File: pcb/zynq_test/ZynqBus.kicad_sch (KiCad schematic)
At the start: 22 parts, among them U202 XC7Z020-2CLG400I

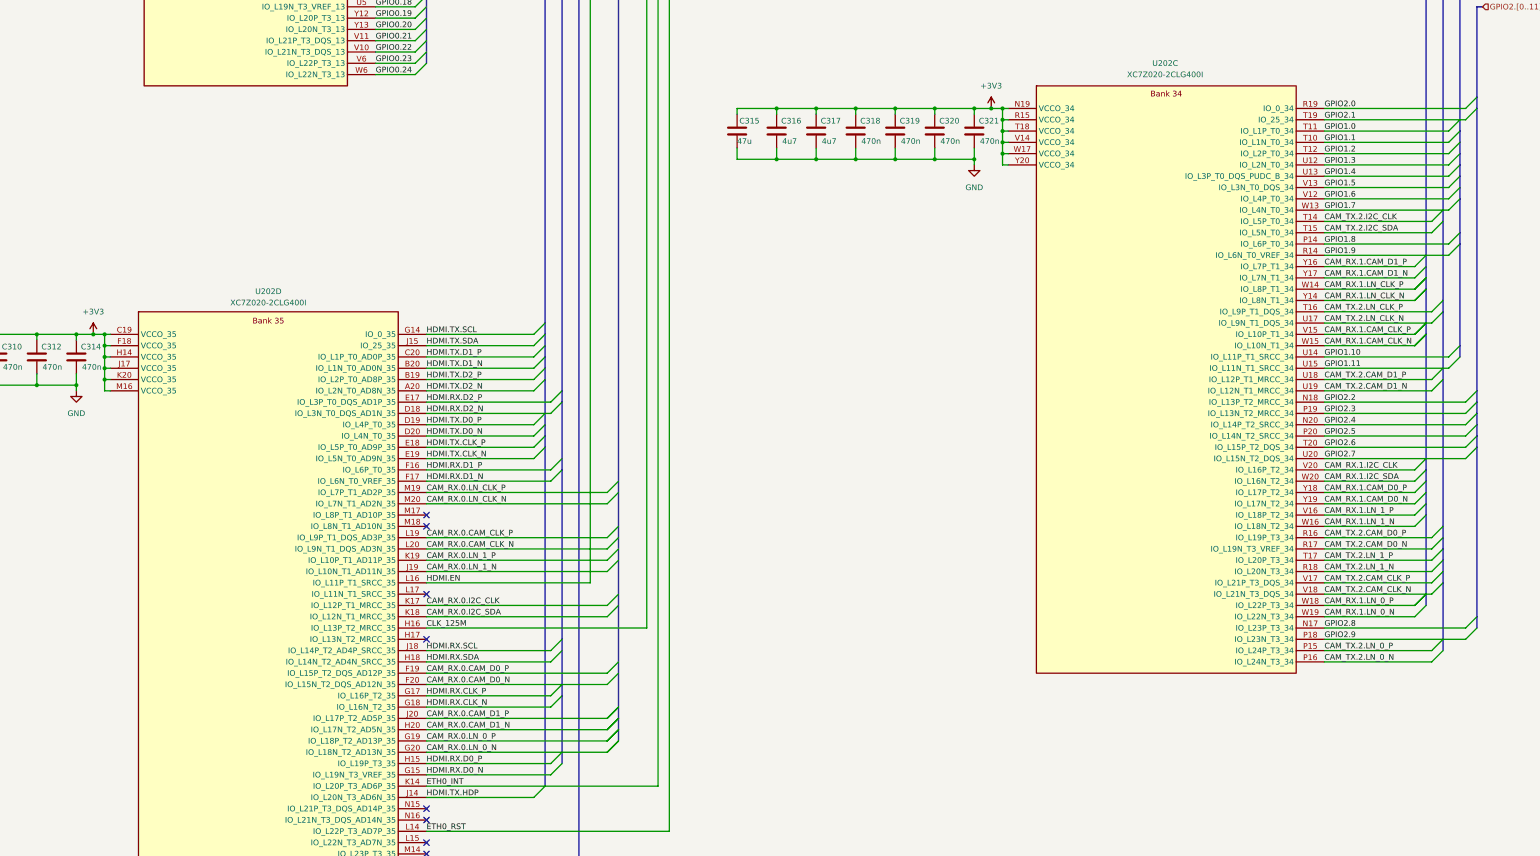
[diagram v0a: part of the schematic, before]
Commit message: finished diff of HDMI
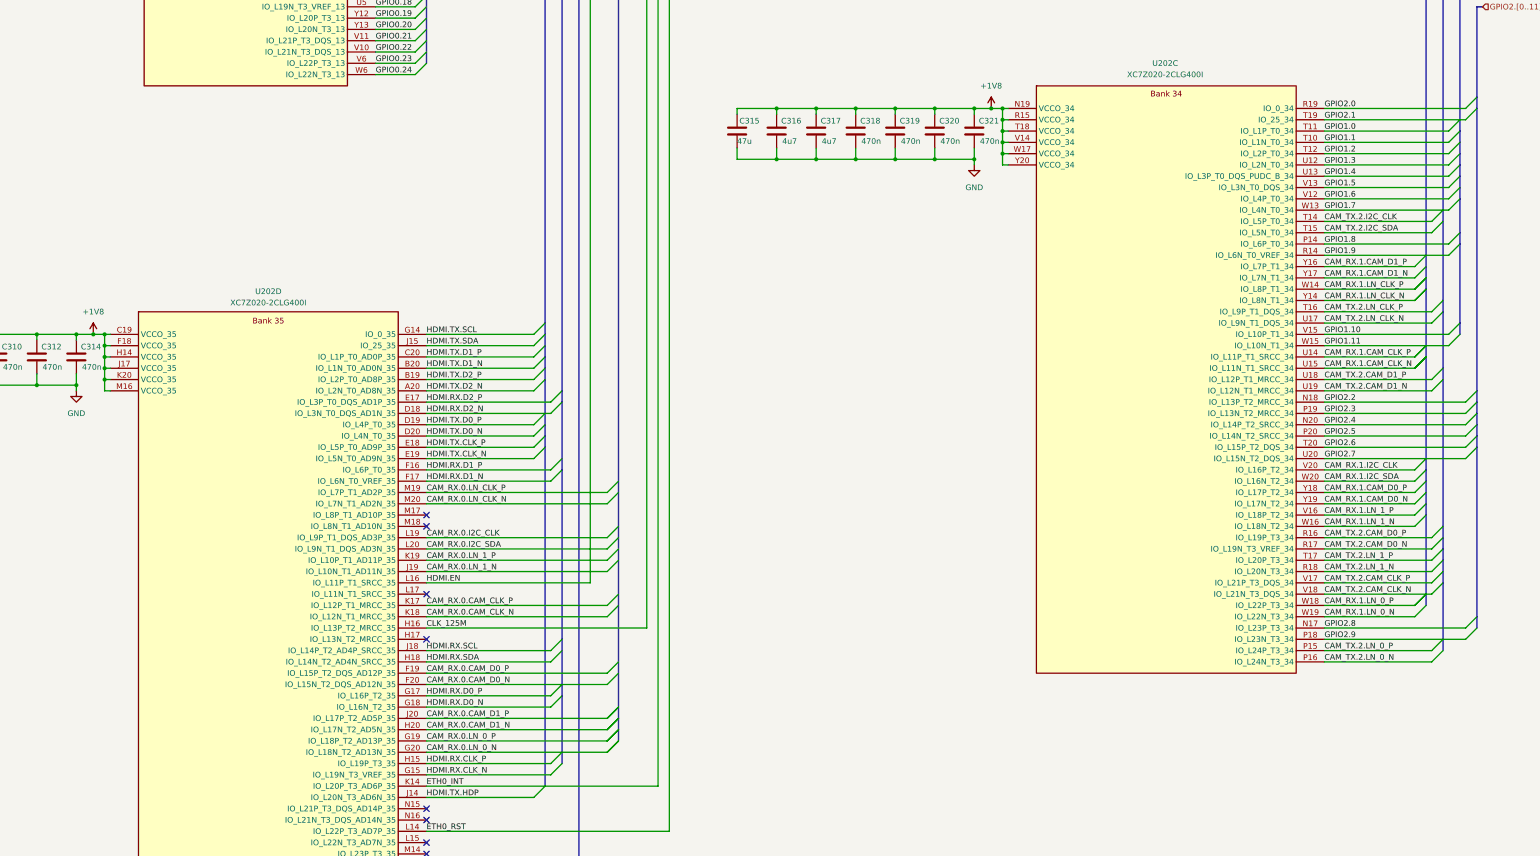
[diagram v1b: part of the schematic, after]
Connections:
- net +3V3 is gone; now on net +1V8: C302.1, C304.1, C306.1, C308.1, C310.1, C312.1, C314.1, C315.1, C316.1, C317.1, C318.1, C319.1, C320.1, C321.1, U202.C19 (VCCO_35), U202.F18 (VCCO_35), U202.H14 (VCCO_35), U202.J17 (VCCO_35), U202.K20 (VCCO_35), U202.M16 (VCCO_35), U202.N19 (VCCO_34), U202.R15 (VCCO_34), U202.T18 (VCCO_34), U202.V14 (VCCO_34), U202.W17 (VCCO_34), U202.Y20 (VCCO_34)
- net CAM_RX.0.CAM_CLK_N: now also U202.K18 (IO_L12N_T1_MRCC_35); no longer U202.L20 (IO_L9N_T1_DQS_AD3N_35)
- net CAM_RX.0.CAM_CLK_P: now also U202.K17 (IO_L12P_T1_MRCC_35); no longer U202.L19 (IO_L9P_T1_DQS_AD3P_35)
- net CAM_RX.0.I2C_CLK: now also U202.L19 (IO_L9P_T1_DQS_AD3P_35); no longer U202.K17 (IO_L12P_T1_MRCC_35)
- net CAM_RX.0.I2C_SDA: now also U202.L20 (IO_L9N_T1_DQS_AD3N_35); no longer U202.K18 (IO_L12N_T1_MRCC_35)
- net CAM_RX.1.CAM_CLK_N: now also U202.U15 (IO_L11N_T1_SRCC_34); no longer U202.W15 (IO_L10N_T1_34)
- net CAM_RX.1.CAM_CLK_P: now also U202.U14 (IO_L11P_T1_SRCC_34); no longer U202.V15 (IO_L10P_T1_34)
- net GPIO1.10: now also U202.V15 (IO_L10P_T1_34); no longer U202.U14 (IO_L11P_T1_SRCC_34)
- net GPIO1.11: now also U202.W15 (IO_L10N_T1_34); no longer U202.U15 (IO_L11N_T1_SRCC_34)
- net HDMI.RX.CLK_N: now also U202.G15 (IO_L19N_T3_VREF_35); no longer U202.G18 (IO_L16N_T2_35)
- net HDMI.RX.CLK_P: now also U202.H15 (IO_L19P_T3_35); no longer U202.G17 (IO_L16P_T2_35)
- net HDMI.RX.D0_N: now also U202.G18 (IO_L16N_T2_35); no longer U202.G15 (IO_L19N_T3_VREF_35)
- net HDMI.RX.D0_P: now also U202.G17 (IO_L16P_T2_35); no longer U202.H15 (IO_L19P_T3_35)

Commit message: Almost done with BOM
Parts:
- C301: renamed from C302; footprint (none) -> Capacitor_SMD:C_1210_3225Metric
- C302: renamed from C301; footprint (none) -> Capacitor_SMD:C_1210_3225Metric
- C303: renamed from C304; footprint (none) -> Capacitor_SMD:C_0402_1005Metric
- C304: renamed from C303; footprint (none) -> Capacitor_SMD:C_0402_1005Metric; now not fitted; now left out of the parts list
- C305: renamed from C306; footprint (none) -> Capacitor_SMD:C_0402_1005Metric
- C306: renamed from C305; footprint (none) -> Capacitor_SMD:C_0402_1005Metric
- C307: renamed from C308; footprint (none) -> Capacitor_SMD:C_0402_1005Metric
- C308: renamed from C307; footprint (none) -> Capacitor_SMD:C_0402_1005Metric
- C309: renamed from C310; footprint (none) -> Capacitor_SMD:C_0402_1005Metric
- C310: renamed from C309; footprint (none) -> Capacitor_SMD:C_0402_1005Metric
- C311: renamed from C312; footprint (none) -> Capacitor_SMD:C_0402_1005Metric
- C312: renamed from C311; footprint (none) -> Capacitor_SMD:C_0402_1005Metric
- C313: renamed from C314; footprint (none) -> Capacitor_SMD:C_0402_1005Metric
- C314: renamed from C313; footprint (none) -> Capacitor_SMD:C_0402_1005Metric
- C315: footprint (none) -> Capacitor_SMD:C_1210_3225Metric
- C316, C317, C318, C319, C320, C321: footprint (none) -> Capacitor_SMD:C_0402_1005Metric
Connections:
- net +1V8: no longer C301.1, C303.1, C305.1, C307.1, C309.1, C311.1, C313.1, U202.C19 (VCCO_35), U202.F18 (VCCO_35), U202.H14 (VCCO_35), U202.J17 (VCCO_35), U202.K20 (VCCO_35), U202.M16 (VCCO_35)
- net CAM_RX.0.I2C_CLK: now also U202.M17 (IO_L8P_T1_AD10P_35); no longer U202.L19 (IO_L9P_T1_DQS_AD3P_35)
- net CAM_RX.0.I2C_SDA: now also U202.M18 (IO_L8N_T1_AD10N_35); no longer U202.L20 (IO_L9N_T1_DQS_AD3N_35)
- net CAM_RX.1.I2C_CLK: now also U202.T14 (IO_L5P_T0_34); no longer U202.V20 (IO_L16P_T2_34)
- net CAM_RX.1.I2C_SDA: now also U202.T15 (IO_L5N_T0_34); no longer U202.W20 (IO_L16N_T2_34)
- net CAM_TX.2.CAM_CLK_N: now also U202.U19 (IO_L12N_T1_MRCC_34); no longer U202.V18 (IO_L21N_T3_DQS_34)
- net CAM_TX.2.CAM_CLK_P: now also U202.U18 (IO_L12P_T1_MRCC_34); no longer U202.V17 (IO_L21P_T3_DQS_34)
- net CAM_TX.2.CAM_D1_N: now also U202.V18 (IO_L21N_T3_DQS_34); no longer U202.U19 (IO_L12N_T1_MRCC_34)
- net CAM_TX.2.CAM_D1_P: now also U202.V17 (IO_L21P_T3_DQS_34); no longer U202.U18 (IO_L12P_T1_MRCC_34)
- net CAM_TX.2.I2C_CLK: now also U202.T16 (IO_L9P_T1_DQS_34); no longer U202.T14 (IO_L5P_T0_34)
- net CAM_TX.2.I2C_SDA: now also U202.U17 (IO_L9N_T1_DQS_34); no longer U202.T15 (IO_L5N_T0_34)
- net CAM_TX.2.LN_CLK_N: now also U202.W20 (IO_L16N_T2_34); no longer U202.U17 (IO_L9N_T1_DQS_34)
- net CAM_TX.2.LN_CLK_P: now also U202.V20 (IO_L16P_T2_34); no longer U202.T16 (IO_L9P_T1_DQS_34)
- net CLK_125M: now also U202.H18 (IO_L14N_T2_AD4N_SRCC_35); no longer U202.H16 (IO_L13P_T2_MRCC_35)
- net HDMI.RX.CLK_N: now also U202.H17 (IO_L13N_T2_MRCC_35); no longer U202.G15 (IO_L19N_T3_VREF_35)
- net HDMI.RX.CLK_P: now also U202.H16 (IO_L13P_T2_MRCC_35); no longer U202.H15 (IO_L19P_T3_35)
- net HDMI.RX.SCL: now also U202.H15 (IO_L19P_T3_35); no longer U202.J18 (IO_L14P_T2_AD4P_SRCC_35)
- net HDMI.RX.SDA: now also U202.G15 (IO_L19N_T3_VREF_35); no longer U202.H18 (IO_L14N_T2_AD4N_SRCC_35)
- net GPIO1.0 renamed CAM_CTR.SCL
- net GPIO1.7 renamed CAM_CTR.SDA
- new net +3V3: C301.1, C303.1, C305.1, C307.1, C309.1, C311.1, C313.1, U202.C19 (VCCO_35), U202.F18 (VCCO_35), U202.H14 (VCCO_35), U202.J17 (VCCO_35), U202.K20 (VCCO_35), U202.M16 (VCCO_35)
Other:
- note added: "Consolidated Cap"

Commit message: Version sent to JLCPCB
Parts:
- C301, C302, C315: JLCPCB Part# (none) -> C525654; PART_NUMBER (none) -> CL32A476KPJNNNE
- C303, C305, C306, C316, C317: JLCPCB Part# (none) -> C23733; PART_NUMBER (none) -> CL05A475MP5NRNC
- C307, C308, C309, C310, C311, C312, C313, C314, C318, C319, C320, C321: JLCPCB Part# (none) -> C88946; PART_NUMBER (none) -> GRM155R71A474KE01D
- U202: JLCPCB Part# (none) -> C569043; PART_NUMBER (none) -> XC7Z020-2CLG400I
